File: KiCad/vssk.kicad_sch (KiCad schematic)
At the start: 148 parts, among them J1 Conn_01x04, SW1 M1, SW10 M10, SW11 `, SW12 Tab, SW13 Stepped Caps, SW14 Capslock, SW15 2.25u Shift, SW16 1.25u Shift, SW17 Ctrl, SW18 1, SW19 Q, SW2 M3, SW20 {backslash}, SW21 2, SW22 W, SW23 A, SW24 Z, SW25 Alt, SW26 3, SW27 E, SW28 S, SW29 X, SW3 M5, SW30 4, SW31 R, SW32 D, SW33 C, SW34 5, SW35 T, SW36 F, SW37 V, SW38 6, SW39 Y, SW4 M7, SW40 G, SW41 B, SW42 7, SW43 U, SW44 H, SW45 N, SW46 10u Space, SW47 7u Space, SW48 8, SW49 I, SW5 M9, SW50 J, SW51 M, SW52 9, SW53 O, SW54 K, SW55 ,, SW56 0, SW57 P, SW58 L, SW59 ., SW6 M2, SW60 -, SW61 [, SW62 ;, SW63 {slash}, SW64 Alt, SW65 =, SW66 ], SW67 ', SW68 2.75u Shift, SW69 1.75u Shift, SW7 M4, SW70 {backslash}, SW71 2u Back, SW72 1u Back, SW73 {backslash}, SW74 Enter, SW75 Fn, SW76 Ctrl, SW77 Insert, SW78 Delete, SW79 Left, SW8 M6, SW80 Home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

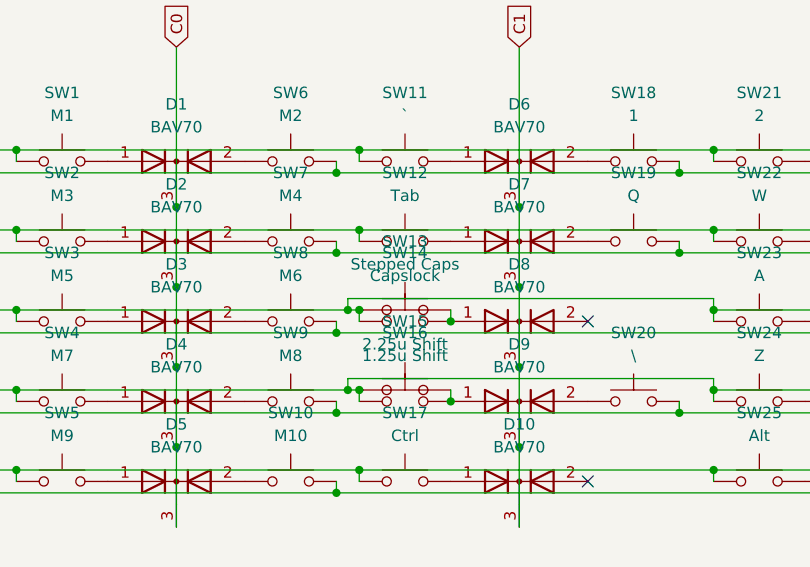
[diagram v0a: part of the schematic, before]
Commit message: placed switch footprints
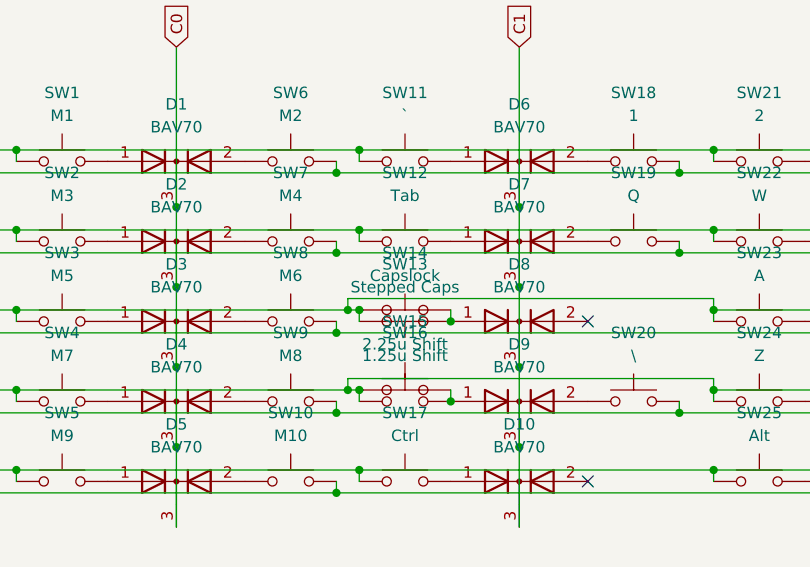
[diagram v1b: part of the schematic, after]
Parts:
- C5, C6, C8: footprint (none) -> keeb:C_0805_2012Metric
- JP1: footprint (none) -> keeb:ResetJumper
- R3, R4: footprint (none) -> keeb:R_0805_2012Metric
- SW1, SW10, SW11, SW18, SW19, SW2, SW20, SW21, SW22, SW23, SW24, SW26, SW27, SW28, SW29, SW3, SW30, SW31, SW32, SW33, SW34, SW35, SW36, SW37, SW38, SW39, SW4, SW40, SW41, SW42, SW43, SW44, SW45, SW48, SW49, SW5, SW50, SW51, SW52, SW53, SW54, SW55, SW56, SW57, SW58, SW59, SW6, SW60, SW61, SW62, SW63, SW65, SW66, SW67, SW7, SW70, SW72, SW75, SW77, SW78, SW79, SW8, SW80, SW81, SW82, SW83, SW84, SW85, SW86, SW9: footprint (none) -> FancyHybridPrints:MX-1U-NoLED
- SW12, SW17, SW25, SW64, SW73, SW76: footprint (none) -> FancyHybridPrints:MX-1.5U-NoLED
- SW13, SW16: footprint (none) -> FancyHybridPrints:MX-1.25U-NoLED
- SW14, SW69: footprint (none) -> FancyHybridPrints:MX-1.75U-NoLED
- SW15, SW74: footprint (none) -> FancyHybridPrints:MX-2.25U-NoLED
- SW46: footprint (none) -> FancyHybridPrints:MX-8U-ReversedStabilizers-NoLED
- SW47: footprint (none) -> FancyHybridPrints:MX-7U-ReversedStabilizers-NoLED
- SW68: footprint (none) -> FancyHybridPrints:MX-2.75U-NoLED
- SW71: footprint (none) -> FancyHybridPrints:MX-2U-NoLED
- U1: footprint Package_QFP:TQFP-44_10x10mm_P0.8mm -> keeb:QFN_TQFP-44_Combined
- Y1: footprint (none) -> keeb:Crystal_SMD_3225-4Pin_3.2x2.5mm_HandSoldering
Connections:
- net R4: now also SW13.2; no longer SW13.1
- net at D8.1 (A), SW14.2: now also SW13.1; no longer SW13.2
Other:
- moved on the sheet: SW13

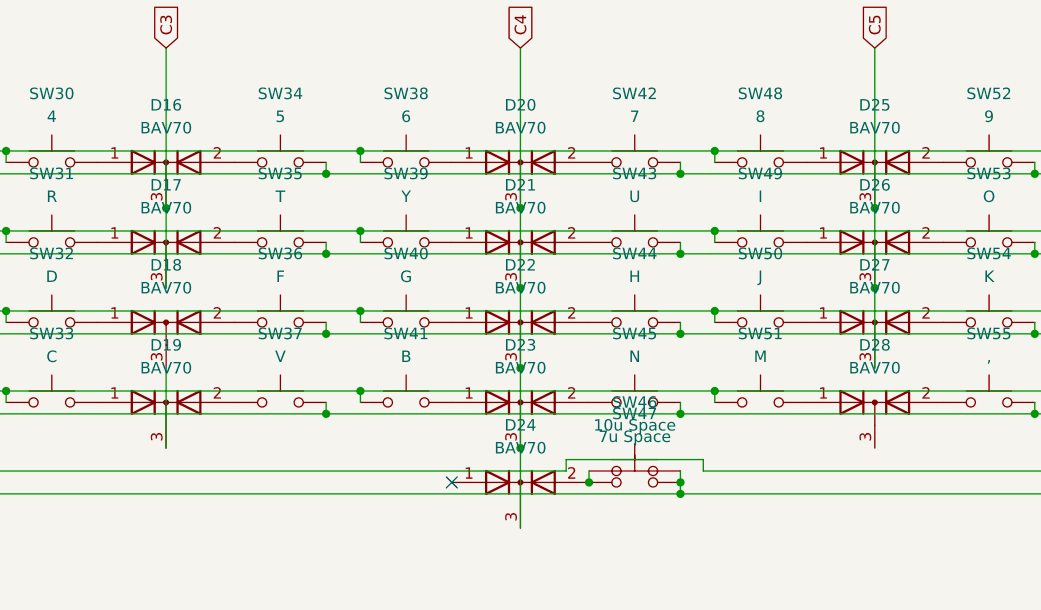
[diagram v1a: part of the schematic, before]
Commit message: placed/routed diodes
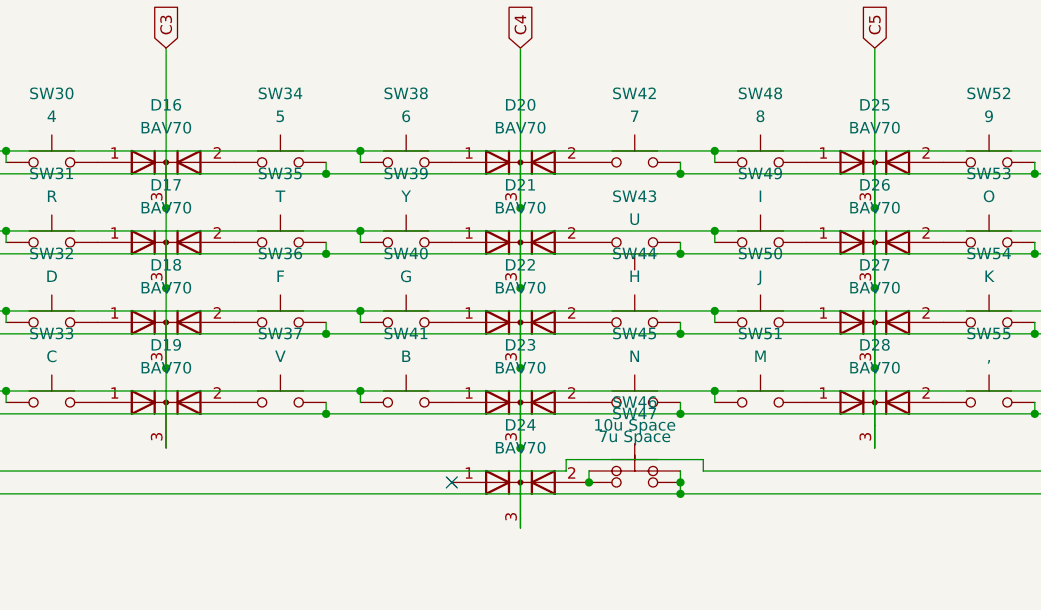
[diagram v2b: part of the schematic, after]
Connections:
- net C3: now also D18.3 (K), D19.3 (K)
- net C5: now also D28.3 (K)
- net R3: now also SW43.2; no longer SW43.1
- net at D21.2 (A): now also SW43.1; no longer SW43.2
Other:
- moved on the sheet: SW43
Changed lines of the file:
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@@
   (junction (at 208.28 63.5) (diameter 0.9144) (color 0 0 0 0))
   (junction (at 226.06 43.18) (diameter 0.9144) (color 0 0 0 0))
+  (junction (at 226.06 52.07) (diameter 0.9144) (color 0 0 0 0))
+  (junction (at 226.06 60.96) (diameter 0.9144) (color 0 0 0 0))
   (junction (at 243.84 39.37) (diameter 0.9144) (color 0 0 0 0))
   (junction (at 243.84 48.26) (diameter 0.9144) (color 0 0 0 0))
@@
   (junction (at 304.8 43.18) (diameter 0.9144) (color 0 0 0 0))
   (junction (at 304.8 52.07) (diameter 0.9144) (color 0 0 0 0))
+  (junction (at 304.8 60.96) (diameter 0.9144) (color 0 0 0 0))
   (junction (at 322.58 39.37) (diameter 0.9144) (color 0 0 0 0))
   (junction (at 322.58 48.26) (diameter 0.9144) (color 0 0 0 0))
@@
     (stroke (width 0) (type solid) (color 0 0 0 0))
   )
+  (wire (pts (xy 226.06 52.07) (xy 226.06 60.96))
+    (stroke (width 0) (type solid) (color 0 0 0 0))
+  )
   (wire (pts (xy 226.06 60.96) (xy 226.06 69.85))
     (stroke (width 0) (type solid) (color 0 0 0 0))
@@
   )
   (wire (pts (xy 304.8 52.07) (xy 304.8 60.96))
+    (stroke (width 0) (type solid) (color 0 0 0 0))
+  )
+  (wire (pts (xy 304.8 60.96) (xy 304.8 69.85))
     (stroke (width 0) (type solid) (color 0 0 0 0))
   )
@@
     (pin "2")
   )
-  (symbol (lib_id "Switch:SW_Push") (at 278.13 46.99 0) (mirror y) (unit 1)
-    (in_bom yes) (on_board yes) (fields_autoplaced)
-    (property "Reference" "SW43" (id 0) (at 278.13 39.37 0))
-    (property "Value" "U" (id 1) (at 278.13 41.91 0))
-    (property "Footprint" "FancyHybridPrints:MX-1U-NoLED" (id 2) (at 278.13 41.91 0)
-      (effects (font (size 1.27 1.27)) hide)
-    )
-    (property "Datasheet" "~" (id 3) (at 278.13 41.91 0)
+  (symbol (lib_id "Switch:SW_Push") (at 278.13 46.99 0) (mirror x) (unit 1)
+    (in_bom yes) (on_board yes) (fields_autoplaced)
+    (property "Reference" "SW43" (id 0) (at 278.13 41.91 0))
+    (property "Value" "U" (id 1) (at 278.13 44.45 0))
+    (property "Footprint" "FancyHybridPrints:MX-1U-NoLED" (id 2) (at 278.13 52.07 0)
+      (effects (font (size 1.27 1.27)) hide)
+    )
+    (property "Datasheet" "~" (id 3) (at 278.13 52.07 0)
       (effects (font (size 1.27 1.27)) hide)
     )
@@
   )
   (symbol (lib_id "Diode:BAV70") (at 226.06 55.88 0) (unit 1)
-    (in_bom yes) (on_board yes) (fields_autoplaced)
+    (in_bom yes) (on_board yes)
     (property "Reference" "D18" (id 0) (at 226.06 49.53 0))
     (property "Value" "BAV70" (id 1) (at 226.06 52.07 0))

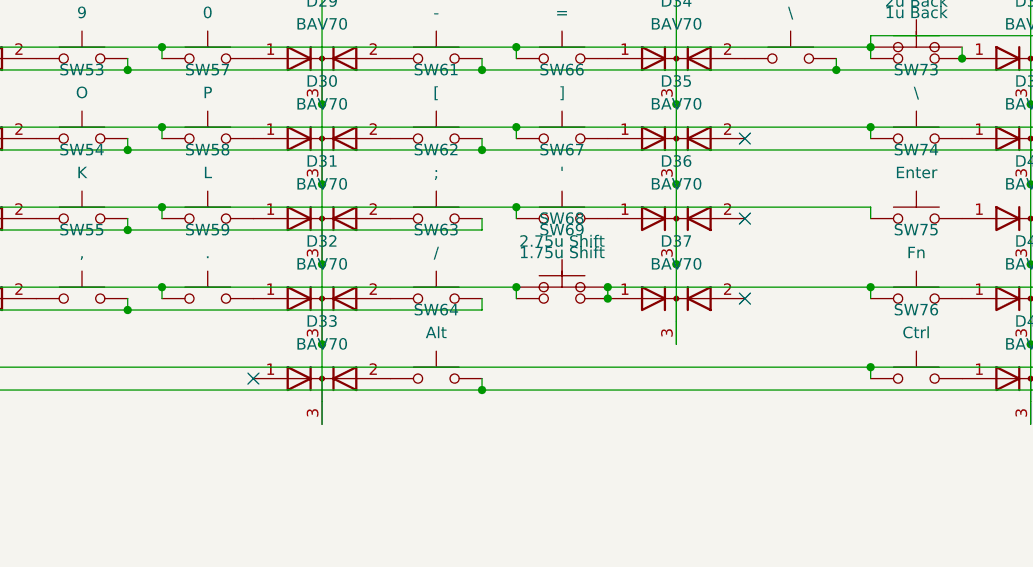
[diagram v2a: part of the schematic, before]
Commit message: routed rows/cols
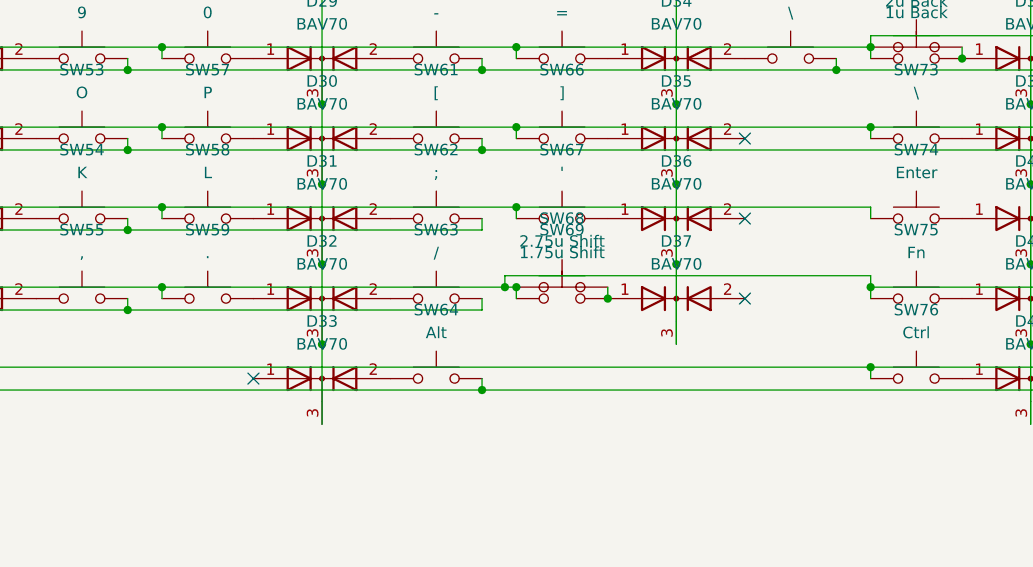
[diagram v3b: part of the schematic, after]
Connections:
- net R6: now also SW75.1, SW82.1
- net at D37.1 (A), SW68.2, SW69.2: no longer SW75.1, SW82.1
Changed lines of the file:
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@@
   (junction (at 361.95 48.26) (diameter 0.9144) (color 0 0 0 0))
   (junction (at 361.95 74.93) (diameter 0.9144) (color 0 0 0 0))
+  (junction (at 364.49 63.5) (diameter 0.9144) (color 0 0 0 0))
   (junction (at 365.76 36.83) (diameter 0.9144) (color 0 0 0 0))
   (junction (at 365.76 45.72) (diameter 0.9144) (color 0 0 0 0))
   (junction (at 365.76 54.61) (diameter 0.9144) (color 0 0 0 0))
   (junction (at 365.76 63.5) (diameter 0.9144) (color 0 0 0 0))
-  (junction (at 375.92 63.5) (diameter 0.9144) (color 0 0 0 0))
   (junction (at 375.92 64.77) (diameter 0.9144) (color 0 0 0 0))
   (junction (at 383.54 43.18) (diameter 0.9144) (color 0 0 0 0))
@@
     (stroke (width 0) (type solid) (color 0 0 0 0))
   )
-  (wire (pts (xy 326.39 63.5) (xy 365.76 63.5))
+  (wire (pts (xy 326.39 63.5) (xy 364.49 63.5))
     (stroke (width 0) (type solid) (color 0 0 0 0))
   )
@@
     (stroke (width 0) (type solid) (color 0 0 0 0))
   )
+  (wire (pts (xy 364.49 62.23) (xy 405.13 62.23))
+    (stroke (width 0) (type solid) (color 0 0 0 0))
+  )
+  (wire (pts (xy 364.49 63.5) (xy 364.49 62.23))
+    (stroke (width 0) (type solid) (color 0 0 0 0))
+  )
+  (wire (pts (xy 364.49 63.5) (xy 365.76 63.5))
+    (stroke (width 0) (type solid) (color 0 0 0 0))
+  )
   (wire (pts (xy 365.76 36.83) (xy 365.76 38.1))
     (stroke (width 0) (type solid) (color 0 0 0 0))
@@
     (stroke (width 0) (type solid) (color 0 0 0 0))
   )
-  (wire (pts (xy 405.13 63.5) (xy 375.92 63.5))
-    (stroke (width 0) (type solid) (color 0 0 0 0))
-  )
+  (wire (pts (xy 405.13 62.23) (xy 405.13 63.5))
+    (stroke (width 0) (type solid) (color 0 0 0 0))
+  )
